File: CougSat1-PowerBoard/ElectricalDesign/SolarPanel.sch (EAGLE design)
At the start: 101 parts, among them J1 Wire Harness Connector, U1 SPV1040, U2 SPV1040, U3 TCA9535R, U4 LTC2499, U5 LTC2499, U6 MCP1501-18

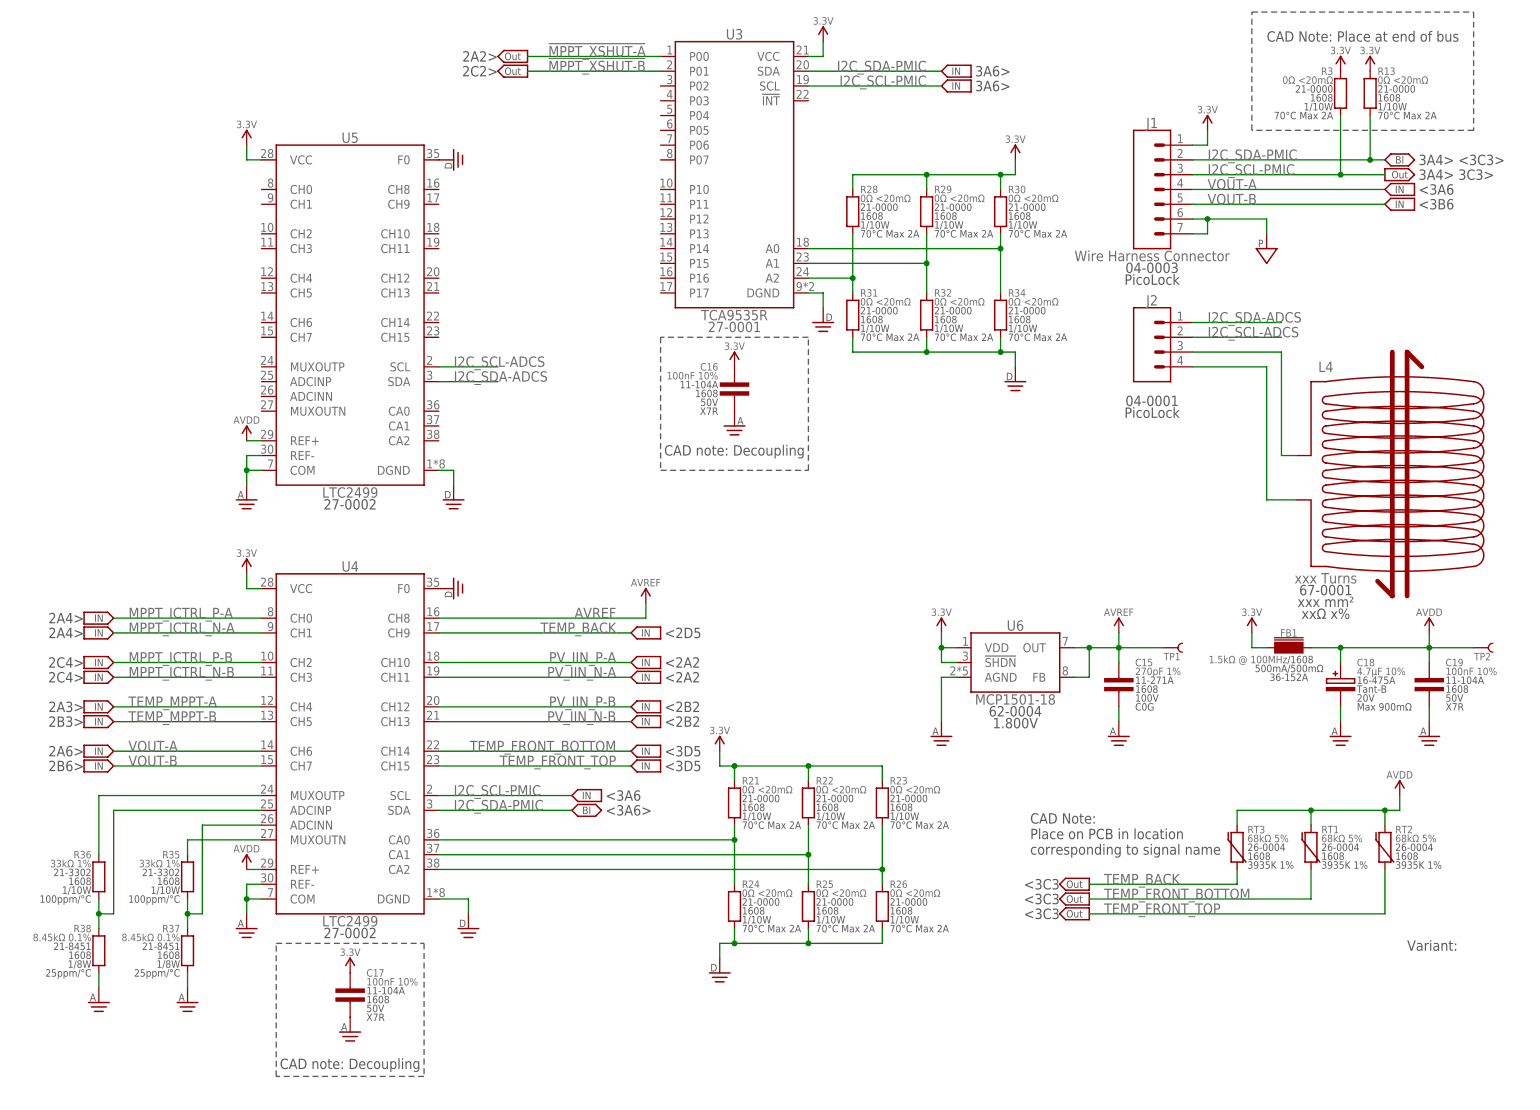
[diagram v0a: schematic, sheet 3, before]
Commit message: Added Second ADC
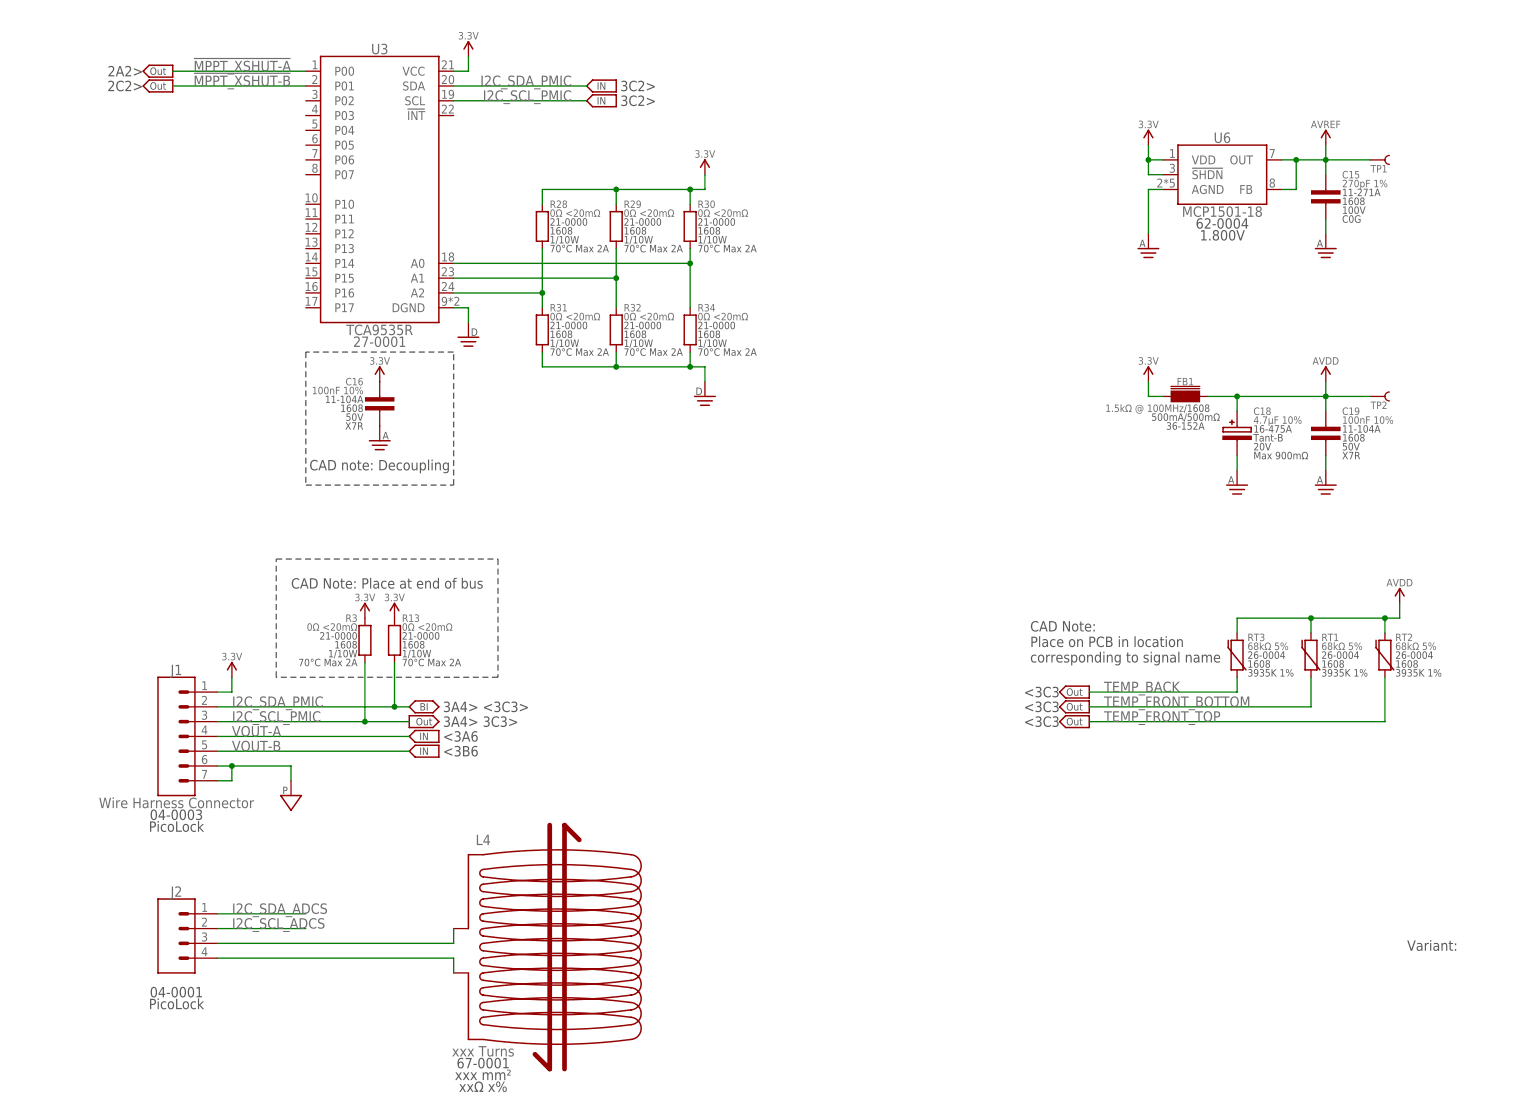
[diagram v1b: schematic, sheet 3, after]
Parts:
- added C26: 100nF 10%, CougsInSpace-Capacitors:CAP-V-100NF-1608
- added R48, R49, R50, R51, R52, R53: 0Ω <20mΩ, CougsInSpace-Resistors:RES-V-0-1608
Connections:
- net ADC_CA0 renamed ADC_EPS_CA0
- net ADC_CA1 renamed ADC_EPS_CA1
- net ADC_CA2 renamed ADC_EPS_CA2
- net I2C_SCL-ADCS renamed I2C_SCL_ADCS
- net I2C_SCL-PMIC renamed I2C_SCL_PMIC
- net I2C_SDA-ADCS renamed I2C_SDA_ADCS
- net I2C_SDA-PMIC renamed I2C_SDA_PMIC
- net N$1 renamed ADC_EPS_ADCINN
- net N$2 renamed ADC_EPS-MUXOUTN
- net N$3 renamed ADC_EPS_ADCINP
- net N$4 renamed ADC_EPS_MUXOUTP
- new net ADC_ADCS_CA0: R48.1, R51.2, U5.CA0
- new net ADC_ADCS_CA1: R49.1, R52.2, U5.CA1
- new net ADC_ADCS_CA2: R50.1, R53.2, U5.CA2
- new net N$6: U5.ADCINP, U5.MUXOUTP
- new net N$7: U5.ADCINN, U5.MUXOUTN
- net 3.3V: now also C26.1, R48.2, R49.2, R50.2
- net AGND: now also C26.2
- net DGND: now also R51.1, R52.1, R53.1
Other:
- note added: "3C2>"
- note added: "3C2> 4A1>"
- note added: "4A1>"
- note added: "4A3>"
- note added: "<4A1"
- note removed: "3A6>"
- note removed: "3C1> 3A6>"
- note removed: "3C3>"
- note removed: "<3C1"
- moved on the sheet: C15, C16, C18, C19, FB1, J1, J2, L4, R13, R28, R29, R3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

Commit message: Updated Block Diagram
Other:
- note added: "Connector: To ADCS"
- note added: "Page 4"
- note removed: "From ADCS"

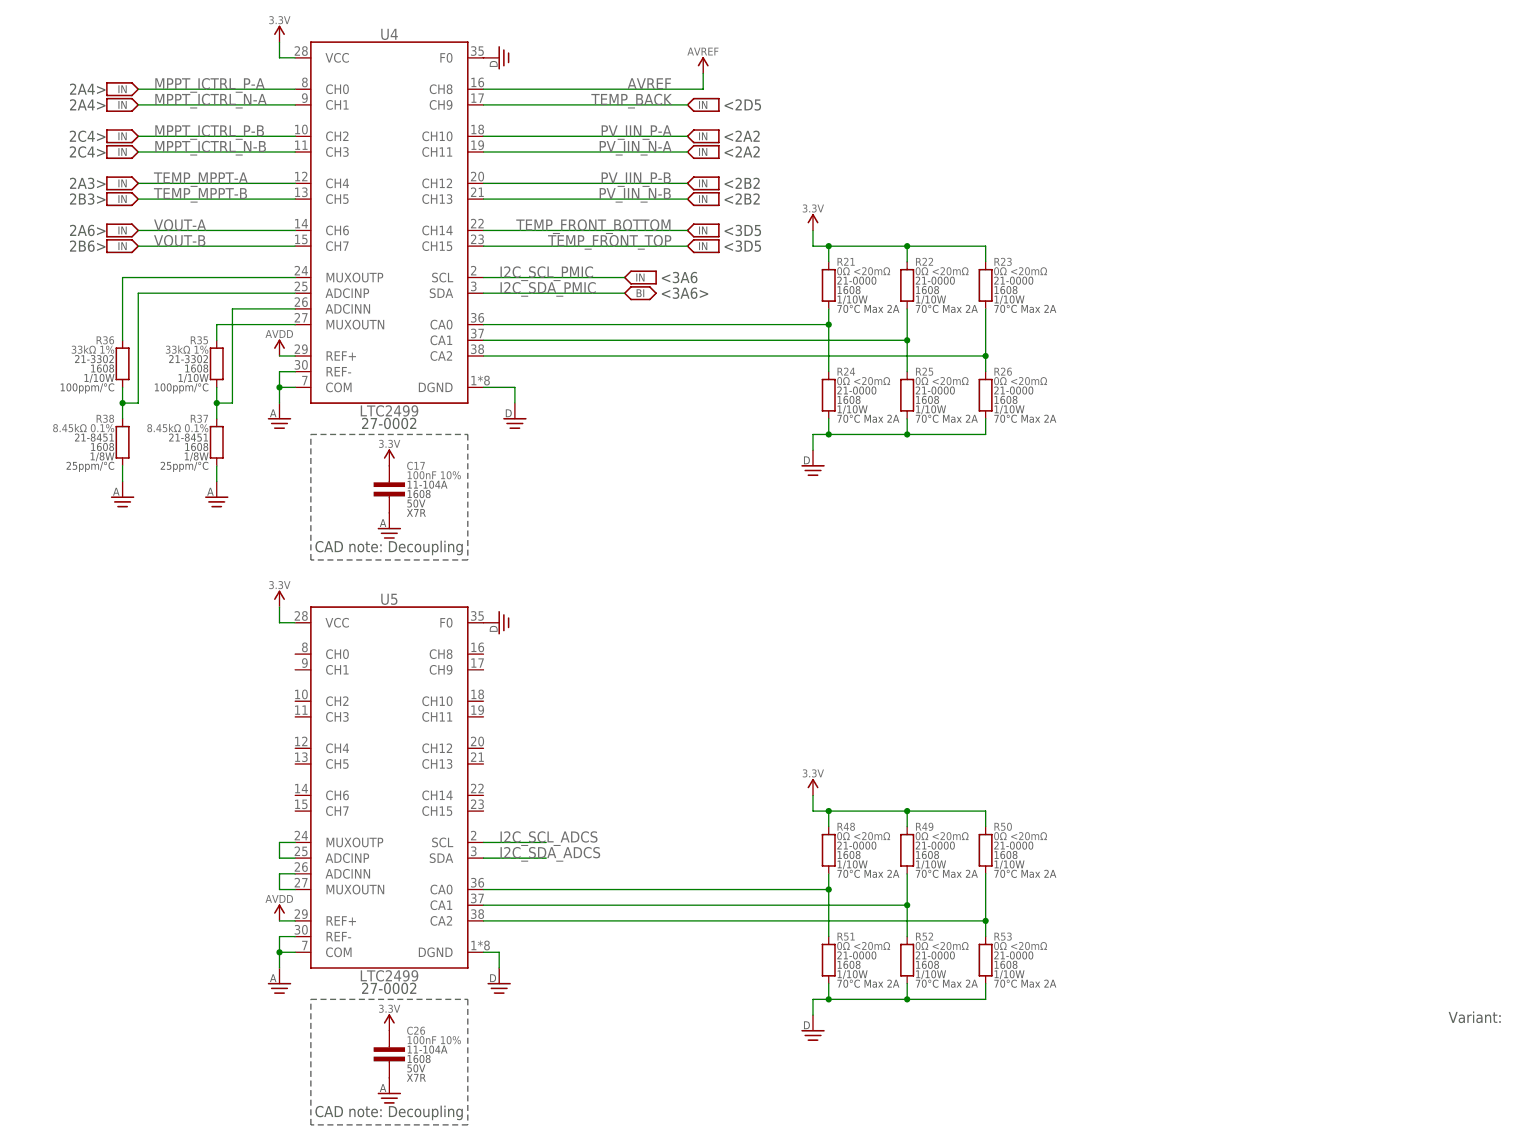
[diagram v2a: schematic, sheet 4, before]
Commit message: Rough Locations for Battery Chargers, Connectors, GPIO
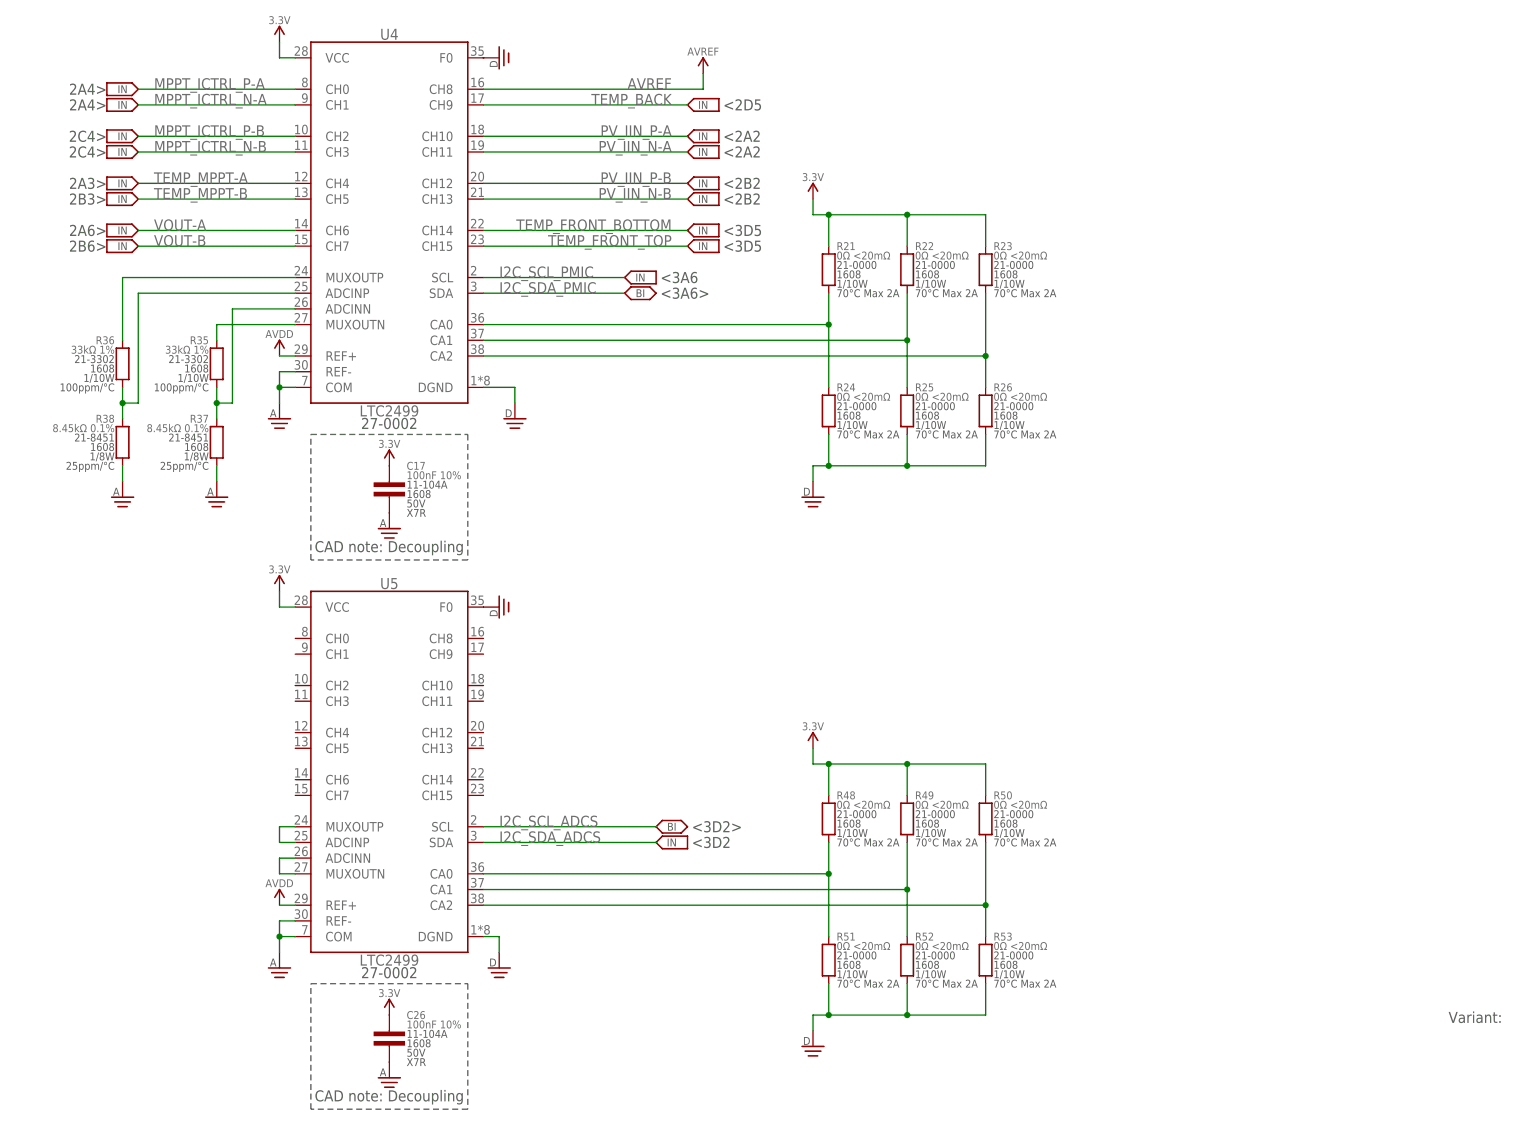
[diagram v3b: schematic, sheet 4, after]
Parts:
- added R54, R55: 0Ω <20mΩ, CougsInSpace-Resistors:RES-V-0-1608
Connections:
- net N$5 renamed MAGNETORQUER-IN
- net N$6 renamed ADC_ADCS_MUXOUTP
- net N$7 renamed ADC_ADCS_MUXOUTN
- net N$8 renamed MAGNETORQUER_OUT
- net 3.3V: now also R54.2, R55.2
- net I2C_SCL_ADCS: now also R54.1
- net I2C_SDA_ADCS: now also R55.1
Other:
- note added: "4C3>"
- note added: "<3D2"
- note added: "<3D2>"
- note added: "<4C3>"
- moved on the sheet: C26, J1, L4, R13, R21, R22, R23, R24, R25, R26, R28, R29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

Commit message: Worked on Routing
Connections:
- net AGND: no longer C16.2, C17.2, C26.2
- net DGND: now also C16.2, C17.2, C26.2
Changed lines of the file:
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@@
 <part name="C16" library="CougsInSpace-Capacitors" deviceset="CAP-V" device="-1608" technology="-100NF" value="100nF 10%"/>
 <part name="SUPPLY26" library="CougsInSpace-PowerSymbols" deviceset="3.3V" device=""/>
-<part name="SUPPLY27" library="CougsInSpace-PowerSymbols" deviceset="AGND" device=""/>
 <part name="FRAME4" library="CougsInSpace-Aesthetics" deviceset="FRAME-A" device="">
 <attribute name="TITLE" value="ADCs"/>
@@
 <part name="C17" library="CougsInSpace-Capacitors" deviceset="CAP-V" device="-1608" technology="-100NF" value="100nF 10%"/>
 <part name="SUPPLY29" library="CougsInSpace-PowerSymbols" deviceset="3.3V" device=""/>
-<part name="SUPPLY30" library="CougsInSpace-PowerSymbols" deviceset="AGND" device=""/>
 <part name="SUPPLY32" library="CougsInSpace-PowerSymbols" deviceset="AGND" device=""/>
 <part name="OFFSHEET20" library="CougsInSpace-Aesthetics" deviceset="OFF_SHEET-IN" device=""/>
@@
 <part name="C26" library="CougsInSpace-Capacitors" deviceset="CAP-V" device="-1608" technology="-100NF" value="100nF 10%"/>
 <part name="SUPPLY77" library="CougsInSpace-PowerSymbols" deviceset="3.3V" device=""/>
-<part name="SUPPLY78" library="CougsInSpace-PowerSymbols" deviceset="AGND" device=""/>
 <part name="DIA4" library="CougsInSpace-Aesthetics" deviceset="DIAGRAM-CONNECT_DOT" device=""/>
 <part name="OFFSHEET13" library="CougsInSpace-Aesthetics" deviceset="OFF_SHEET-OUT" device=""/>
@@
 <part name="SUPPLY79" library="CougsInSpace-PowerSymbols" deviceset="3.3V" device=""/>
 <part name="SUPPLY80" library="CougsInSpace-PowerSymbols" deviceset="3.3V" device=""/>
+<part name="SUPPLY27" library="CougsInSpace-PowerSymbols" deviceset="DGND" device=""/>
+<part name="SUPPLY30" library="CougsInSpace-PowerSymbols" deviceset="DGND" device=""/>
+<part name="SUPPLY78" library="CougsInSpace-PowerSymbols" deviceset="DGND" device=""/>
 </parts>
 <sheets>
@@
 <attribute name="VALUE" x="60.96" y="128.016" size="1.27" layer="96" rot="MR0" align="center"/>
 </instance>
-<instance part="SUPPLY27" gate="G$1" x="60.96" y="114.3" smashed="yes" rot="MR0"/>
 <instance part="R28" gate="G$1" x="88.9" y="152.4" smashed="yes">
 <attribute name="NAME" x="90.17" y="157.48" size="1.27" layer="95" align="center-left"/>
@@
 <attribute name="VALUE" x="73.66" y="54.356" size="1.27" layer="96" align="center"/>
 </instance>
+<instance part="SUPPLY27" gate="1" x="60.96" y="114.3" smashed="yes"/>
 </instances>
 <busses>
@@
 <wire x1="116.84" y1="121.92" x2="116.84" y2="119.38" width="0.1524" layer="91"/>
 </segment>
+<segment>
+<pinref part="C16" gate="G$1" pin="2"/>
+<pinref part="SUPPLY27" gate="1" pin="DGND"/>
+</segment>
 </net>
 <net name="AGND" class="0">
@@
 <pinref part="SUPPLY35" gate="G$1" pin="AGND"/>
 <wire x1="208.28" y1="109.22" x2="208.28" y2="111.76" width="0.1524" layer="91"/>
-</segment>
-<segment>
-<pinref part="C16" gate="G$1" pin="2"/>
-<pinref part="SUPPLY27" gate="G$1" pin="AGND"/>
 </segment>
 <segment>
@@
 <attribute name="VALUE" x="66.04" y="120.396" size="1.27" layer="96" align="center"/>
 </instance>
-<instance part="SUPPLY30" gate="G$1" x="66.04" y="106.68" smashed="yes"/>
 <instance part="SUPPLY32" gate="G$1" x="48.26" y="124.46" smashed="yes"/>
 <instance part="OFFSHEET20" gate="G$1" x="116.84" y="167.64" smashed="yes" rot="MR0"/>
@@
 <attribute name="VALUE" x="66.04" y="31.496" size="1.27" layer="96" align="center"/>
 </instance>
-<instance part="SUPPLY78" gate="G$1" x="66.04" y="17.78" smashed="yes"/>
 <instance part="OFFSHEET45" gate="G$1" x="111.76" y="58.42" smashed="yes"/>
 <instance part="OFFSHEET46" gate="G$1" x="111.76" y="55.88" smashed="yes" rot="MR0"/>
+<instance part="SUPPLY30" gate="1" x="66.04" y="106.68" smashed="yes"/>
+<instance part="SUPPLY78" gate="1" x="66.04" y="17.78" smashed="yes"/>
 </instances>
 <busses>
@@
 <wire x1="134.62" y1="27.94" x2="134.62" y2="25.4" width="0.1524" layer="91"/>
 </segment>
+<segment>
+<pinref part="C17" gate="G$1" pin="2"/>
+<pinref part="SUPPLY30" gate="1" pin="DGND"/>
+</segment>
+<segment>
+<pinref part="C26" gate="G$1" pin="2"/>
+<pinref part="SUPPLY78" gate="1" pin="DGND"/>
+</segment>
 </net>
 <net name="AGND" class="0">
@@
 </segment>
 <segment>
-<pinref part="C17" gate="G$1" pin="2"/>
-<pinref part="SUPPLY30" gate="G$1" pin="AGND"/>
-</segment>
-<segment>
 <pinref part="SUPPLY32" gate="G$1" pin="AGND"/>
 <wire x1="48.26" y1="127" x2="48.26" y2="129.54" width="0.1524" layer="91"/>
@@
 <pinref part="SUPPLY43" gate="G$1" pin="AGND"/>
 </segment>
-<segment>
-<pinref part="C26" gate="G$1" pin="2"/>
-<pinref part="SUPPLY78" gate="G$1" pin="AGND"/>
-</segment>
-</net>
+</net>

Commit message: Routed MPPTs, part of ADC
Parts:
- added C27, C28: 4.7µF 10%, CougsInSpace-Capacitors:CAP-V-4.7UF-3216
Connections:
- new net OUTPUT_CAP-A: C2.2, C27.1
- new net OUTPUT_CAP-B: C28.1, C9.2
- net !MPPT_XSHUT-A: now also U3.P01; no longer U3.P00
- net !MPPT_XSHUT-B: now also U3.P00; no longer U3.P01
- net AVREF: now also U4.CH7; no longer U4.CH8
- net MPPT_ICTRL_N-A: now also U4.CH0; no longer U4.CH1
- net MPPT_ICTRL_N-B: now also U4.CH8; no longer U4.CH3
- net MPPT_ICTRL_P-A: now also U4.CH1; no longer U4.CH0
- net MPPT_ICTRL_P-B: now also U4.CH9; no longer U4.CH2
- net PGND: now also C27.2, C28.2; no longer C2.2, C9.2
- net PV_IIN_N-A: now also U4.CH2; no longer U4.CH11
- net PV_IIN_N-B: now also U4.CH5; no longer U4.CH13
- net PV_IIN_P-A: now also U4.CH3; no longer U4.CH10
- net PV_IIN_P-B: now also U4.CH4; no longer U4.CH12
- net TEMP_BACK: now also U4.CH6; no longer U4.CH9
- net TEMP_MPPT-A: now also U4.CH12; no longer U4.CH4
- net TEMP_MPPT-B: now also U4.CH13; no longer U4.CH5
- net VOUT-A: now also U4.CH11; no longer U4.CH6
- net VOUT-B: now also U4.CH10; no longer U4.CH7
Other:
- moved on the sheet: C2, C9
